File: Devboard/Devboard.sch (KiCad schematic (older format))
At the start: 49 parts, among them J1 9V DC, J2 In 3.5mm, J3 In 6.3mm, J4 Out 3.5mm, J5 Out 6.3mm, J6 I/O, J7 Power In, J8 Power Out, SW1 On/Off, SW3 Input Clipping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

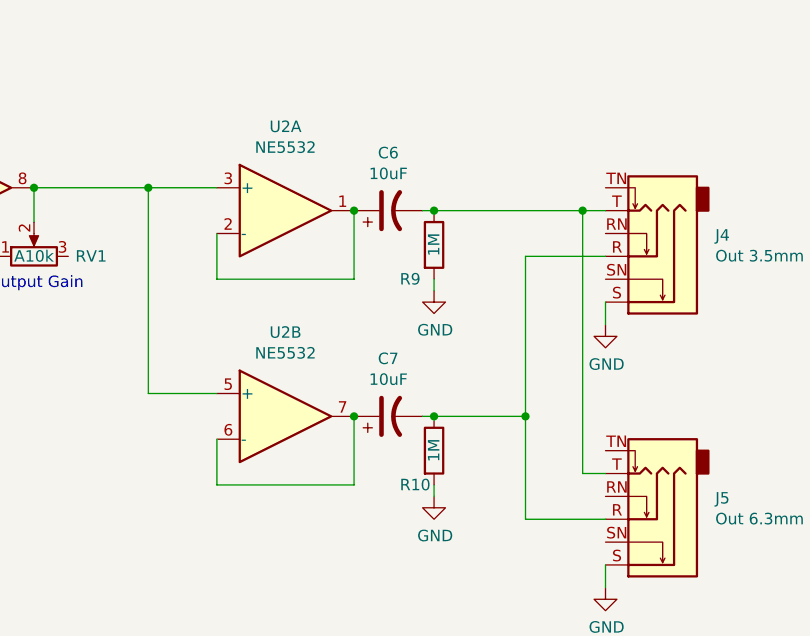
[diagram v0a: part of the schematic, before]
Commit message: Devboard iteration, change output filter values
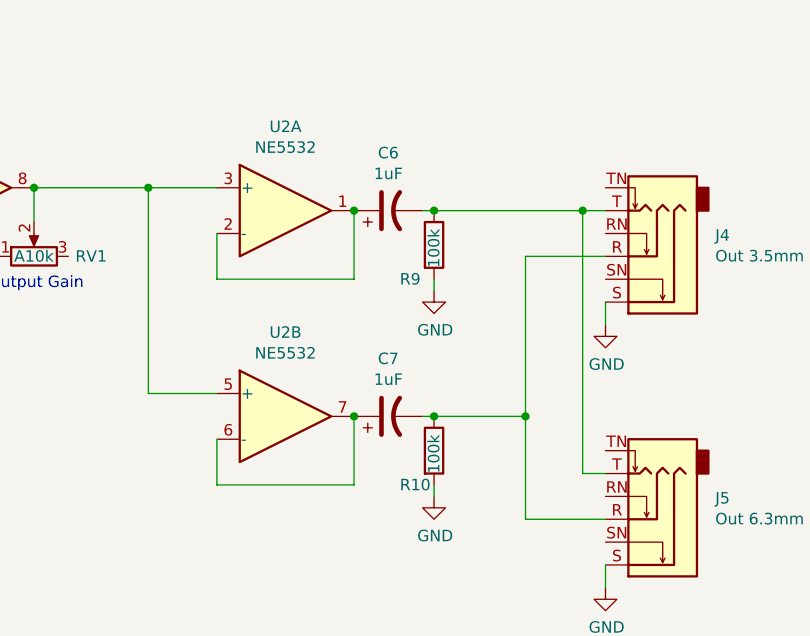
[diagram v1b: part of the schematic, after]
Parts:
- C6, C7: value 10uF -> 1uF
- R10, R9: value 1M -> 100k
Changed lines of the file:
@@
 P 3550 6050
 F 0 "R9" H 3400 5900 50  0000 L CNN
-F 1 "1M" V 3550 6000 50  0000 L CNN
+F 1 "100k" V 3550 5950 50  0000 L CNN
 F 2 "Resistor_THT:R_Axial_DIN0207_L6.3mm_D2.5mm_P10.16mm_Horizontal" V 3480 6050 50  0001 C CNN
 F 3 "~" H 3550 6050 50  0001 C CNN
@@
 P 3350 5900
 F 0 "C6" V 3602 5900 50  0000 C CNN
-F 1 "10uF" V 3511 5900 50  0000 C CNN
+F 1 "1uF" V 3511 5900 50  0000 C CNN
 F 2 "" H 3350 5900 50  0001 C CNN
 F 3 "~" H 3350 5900 50  0001 C CNN
@@
 P 3550 6950
 F 0 "R10" H 3400 6800 50  0000 L CNN
-F 1 "1M" V 3550 6900 50  0000 L CNN
+F 1 "100k" V 3550 6850 50  0000 L CNN
 F 2 "Resistor_THT:R_Axial_DIN0207_L6.3mm_D2.5mm_P10.16mm_Horizontal" V 3480 6950 50  0001 C CNN
 F 3 "~" H 3550 6950 50  0001 C CNN
@@
 P 3350 6800
 F 0 "C7" V 3602 6800 50  0000 C CNN
-F 1 "10uF" V 3511 6800 50  0000 C CNN
+F 1 "1uF" V 3511 6800 50  0000 C CNN
 F 2 "" H 3350 6800 50  0001 C CNN
 F 3 "~" H 3350 6800 50  0001 C CNN

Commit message: Devboard iteration
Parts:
- C1, C6, C7: value 1uF -> 100nF
- R10, R9: value 100k -> 1M
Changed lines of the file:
@@
 P 3550 6050
 F 0 "R9" H 3400 5900 50  0000 L CNN
-F 1 "100k" V 3550 5950 50  0000 L CNN
+F 1 "1M" V 3550 6000 50  0000 L CNN
 F 2 "Resistor_THT:R_Axial_DIN0207_L6.3mm_D2.5mm_P10.16mm_Horizontal" V 3480 6050 50  0001 C CNN
 F 3 "~" H 3550 6050 50  0001 C CNN
@@
 P 1750 3150
 F 0 "C1" V 1498 3150 50  0000 C CNN
-F 1 "1uF" V 1589 3150 50  0000 C CNN
+F 1 "100nF" V 1589 3150 50  0000 C CNN
 F 2 "" H 1788 3000 50  0001 C CNN
 F 3 "~" H 1750 3150 50  0001 C CNN
@@
 P 3350 5900
 F 0 "C6" V 3602 5900 50  0000 C CNN
-F 1 "1uF" V 3511 5900 50  0000 C CNN
+F 1 "100nF" V 3511 5900 50  0000 C CNN
 F 2 "" H 3350 5900 50  0001 C CNN
 F 3 "~" H 3350 5900 50  0001 C CNN
@@
 P 3550 6950
 F 0 "R10" H 3400 6800 50  0000 L CNN
-F 1 "100k" V 3550 6850 50  0000 L CNN
+F 1 "1M" V 3550 6900 50  0000 L CNN
 F 2 "Resistor_THT:R_Axial_DIN0207_L6.3mm_D2.5mm_P10.16mm_Horizontal" V 3480 6950 50  0001 C CNN
 F 3 "~" H 3550 6950 50  0001 C CNN
@@
 P 3350 6800
 F 0 "C7" V 3602 6800 50  0000 C CNN
-F 1 "1uF" V 3511 6800 50  0000 C CNN
+F 1 "100nF" V 3511 6800 50  0000 C CNN
 F 2 "" H 3350 6800 50  0001 C CNN
 F 3 "~" H 3350 6800 50  0001 C CNN

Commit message: Just EE things
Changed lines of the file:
@@
 $EndComp
 $Comp
-L Oma:+4.5V #PWR04
+L Devboard-rescue:+4.5V-Oma #PWR04
 U 1 1 603FC9A4
 P 1950 2800
@@
 $EndComp
 $Comp
-L Oma:+4.5V #PWR05
+L Devboard-rescue:+4.5V-Oma #PWR05
 U 1 1 6040A6F4
 P 3150 850
@@
 	3400 3250 3350 3250
 $Comp
-L Oma:+4.5V #PWR08
+L Devboard-rescue:+4.5V-Oma #PWR08
 U 1 1 604D35DC
 P 3400 2900
@@
 Connection ~ 1200 5900
 $Comp
-L Oma:+4.5V #PWR01
+L Devboard-rescue:+4.5V-Oma #PWR01
 U 1 1 605E6B64
 P 1200 5550
@@
 $EndComp
 $Comp
-L Oma:+4.5V #PWR022
+L Devboard-rescue:+4.5V-Oma #PWR022
 U 1 1 605D177A
 P 7600 1100
@@
 $EndComp
 $Comp
-L Oma:+4.5V #PWR025
+L Devboard-rescue:+4.5V-Oma #PWR025
 U 1 1 6059A8B5
 P 8800 1100
@@
 $EndComp
 $Comp
-L Oma:+4.5V #PWR019
+L Devboard-rescue:+4.5V-Oma #PWR019
 U 1 1 605A485E
 P 5950 1100
